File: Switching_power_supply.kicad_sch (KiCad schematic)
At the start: 28 parts, among them J8 Conn_01x03_Pin, SW1 SW_DIP_x04, U4 AMS1117, U5 LM2596HVS-ADJRG

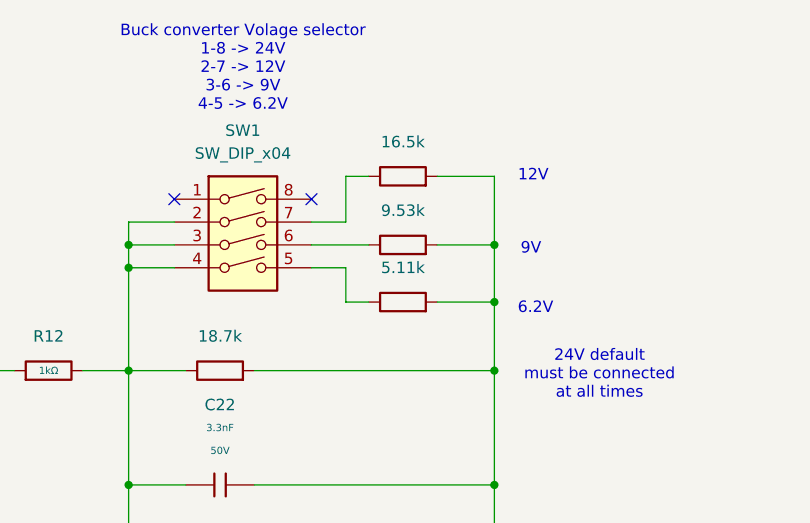
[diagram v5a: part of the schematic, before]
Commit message: Added Routing
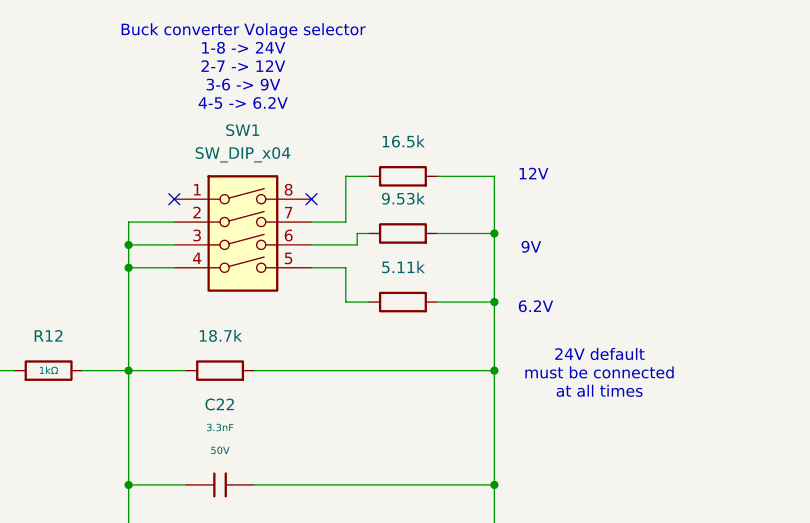
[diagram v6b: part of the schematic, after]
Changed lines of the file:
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@@
 	)
 	(junction
-		(at 195.58 66.04)
+		(at 228.6 111.76)
 		(diameter 0)
 		(color 0 0 0 0)
 	)
 	(junction
-		(at 228.6 111.76)
+		(at 200.66 111.76)
 		(diameter 0)
 		(color 0 0 0 0)
 	)
 	(junction
-		(at 200.66 111.76)
+		(at 158.75 111.76)
 		(diameter 0)
 		(color 0 0 0 0)
 	)
 	(junction
-		(at 158.75 111.76)
+		(at 195.58 64.77)
 		(diameter 0)
 		(color 0 0 0 0)
@@
 	(wire
 		(pts
+			(xy 180.34 66.04) (xy 175.26 66.04)
+		)
+		(stroke
+			(width 0)
+			(type default)
+		)
+	)
+	(wire
+		(pts
 			(xy 212.09 123.19) (xy 212.09 129.54)
 		)
@@
 	(wire
 		(pts
-			(xy 195.58 66.04) (xy 195.58 72.39)
-		)
-		(stroke
-			(width 0)
-			(type default)
-		)
-	)
-	(wire
-		(pts
 			(xy 195.58 111.76) (xy 200.66 111.76)
 		)
@@
 	(wire
 		(pts
-			(xy 189.23 66.04) (xy 195.58 66.04)
+			(xy 189.23 64.77) (xy 195.58 64.77)
 		)
 		(stroke
@@
 	(wire
 		(pts
-			(xy 195.58 58.42) (xy 195.58 66.04)
+			(xy 195.58 58.42) (xy 195.58 64.77)
 		)
 		(stroke
@@
 	(wire
 		(pts
+			(xy 195.58 64.77) (xy 195.58 72.39)
+		)
+		(stroke
+			(width 0)
+			(type default)
+		)
+	)
+	(wire
+		(pts
 			(xy 114.3 175.26) (xy 114.3 180.34)
 		)
@@
 	(wire
 		(pts
-			(xy 175.26 66.04) (xy 181.61 66.04)
+			(xy 180.34 64.77) (xy 181.61 64.77)
 		)
 		(stroke
@@
 	(wire
 		(pts
+			(xy 180.34 64.77) (xy 180.34 66.04)
+		)
+		(stroke
+			(width 0)
+			(type default)
+		)
+	)
+	(wire
+		(pts
 			(xy 200.66 129.54) (xy 200.66 135.89)
 		)
@@
 	(symbol
 		(lib_id "Device:R")
-		(at 185.42 66.04 90)
+		(at 185.42 64.77 90)
 		(unit 1)
 		(exclude_from_sim no)
@@
 		(fields_autoplaced yes)
 		(property "Reference" "R15"
-			(at 185.42 59.69 90)
+			(at 185.42 58.42 90)
 			(effects
 				(font
@@
 		)
 		(property "Value" "9.53k"
-			(at 185.42 62.23 90)
+			(at 185.42 60.96 90)
 			(effects
 				(font
@@
 		)
 		(property "Footprint" "PCM_JLCPCB:R_0402"
-			(at 185.42 67.818 90)
+			(at 185.42 66.548 90)
 			(effects
 				(font
@@
 		)
 		(property "Datasheet" "~"
-			(at 185.42 66.04 0)
+			(at 185.42 64.77 0)
 			(effects
 				(font
@@
 		)
 		(property "Description" "Resistor"
-			(at 185.42 66.04 0)
+			(at 185.42 64.77 0)
 			(effects
 				(font
@@
 		)
 		(property "LCSC" "C295883"
-			(at 185.42 66.04 90)
+			(at 185.42 64.77 90)
 			(effects
 				(font
@@
 		)
 		(property "Sim.Device" ""
-			(at 185.42 66.04 90)
+			(at 185.42 64.77 90)
 			(effects
 				(font
@@
 		)
 		(instances
-			(project "MMS2_hat_template_small"
+			(project "MMS3_hat_stepper_controler"
 				(path "/6596548a-44e0-46d8-8624-fd71cf4a3e17/c6fe6645-c1eb-4317-9e6f-134a73c9fa05"
 					(reference "R15")

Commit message: updated routing
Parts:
- added TP8: TestPoint, TestPoint:TestPoint_Pad_D1.0mm, symbol Connector:TestPoint
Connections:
- net U_reg: now also TP8.1
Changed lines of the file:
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@@
 	)
 	(junction
+		(at 259.08 111.76)
+		(diameter 0)
+		(color 0 0 0 0)
+	)
+	(junction
 		(at 106.68 124.46)
 		(diameter 0)
@@
 	(wire
 		(pts
+			(xy 259.08 111.76) (xy 266.7 111.76)
+		)
+		(stroke
+			(width 0)
+			(type default)
+		)
+	)
+	(wire
+		(pts
 			(xy 168.91 80.01) (xy 195.58 80.01)
 		)
@@
 	(wire
 		(pts
-			(xy 250.19 111.76) (xy 256.54 111.76)
+			(xy 250.19 111.76) (xy 259.08 111.76)
 		)
 		(stroke
@@
 	(wire
 		(pts
+			(xy 259.08 109.22) (xy 259.08 111.76)
+		)
+		(stroke
+			(width 0)
+			(type default)
+		)
+	)
+	(wire
+		(pts
 			(xy 200.66 111.76) (xy 212.09 111.76)
 		)
@@
 	(symbol
 		(lib_id "power:+5V")
-		(at 256.54 111.76 270)
+		(at 266.7 111.76 270)
 		(mirror x)
 		(unit 1)
@@
 		(fields_autoplaced yes)
 		(property "Reference" "#PWR090"
-			(at 252.73 111.76 0)
+			(at 262.89 111.76 0)
 			(effects
 				(font
@@
 		)
 		(property "Value" "U_reg"
-			(at 260.35 111.7599 90)
+			(at 270.51 111.7599 90)
 			(effects
 				(font
@@
 		)
 		(property "Footprint" ""
-			(at 256.54 111.76 0)
+			(at 266.7 111.76 0)
 			(effects
 				(font
@@
 		)
 		(property "Datasheet" ""
-			(at 256.54 111.76 0)
+			(at 266.7 111.76 0)
 			(effects
 				(font
@@
 		)
 		(property "Description" "Power symbol creates a global label with name \"+5V\""
-			(at 256.54 111.76 0)
+			(at 266.7 111.76 0)
 			(effects
 				(font
@@
 					(unit 1)
 				)
+			)
+		)
+	)
+	(symbol
+		(lib_id "Connector:TestPoint")
+		(at 259.08 109.22 0)
+		(unit 1)
+		(exclude_from_sim no)
+		(in_bom yes)
+		(on_board yes)
+		(dnp no)
+		(fields_autoplaced yes)
+		(property "Reference" "TP8"
+			(at 261.62 104.6479 0)
+			(effects
+				(font
+					(size 1.27 1.27)
+				)
+				(justify left)
+			)
+		)
+		(property "Value" "TestPoint"
+			(at 261.62 107.1879 0)
+			(effects
+				(font
+					(size 1.27 1.27)
+				)
+				(justify left)
+			)
+		)
+		(property "Footprint" "TestPoint:TestPoint_Pad_D1.0mm"
+			(at 264.16 109.22 0)
+			(effects
+				(font
+					(size 1.27 1.27)
+				)
+				(hide yes)
+			)
+		)
+		(property "Datasheet" "~"
+			(at 264.16 109.22 0)
+			(effects
+				(font
+					(size 1.27 1.27)
+				)
+				(hide yes)
+			)
+		)
+		(property "Description" "test point"
+			(at 259.08 109.22 0)
+			(effects
+				(font
+					(size 1.27 1.27)
+				)
+				(hide yes)
+			)
+		)
+		(pin "1"
+		)
+		(instances
+			(project "MMS3_hat_stepper_controler"
+				(path "/6596548a-44e0-46d8-8624-fd71cf4a3e17/c6fe6645-c1eb-4317-9e6f-134a73c9fa05"
+					(reference "TP8")
+					(unit 1)
+				)

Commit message: minor fixes + production files
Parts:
- added D5, D6, D7: MBRD10100CTTR, SMC_MBRD10100CTTR:TO-252-3_L6.5-W5.8-P4.58-TL, symbol SMC_MBRD10100CTTR:MBRD10100CTTR
- L1: LCSC C5368704 -> C5368704
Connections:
- net U_reg: now also D7.2 (K); no longer J8.3 (Pin_3)
- new net: D6.2 (K), D7.1, D7.3
- new net: D5.1, D5.3, J8.3 (Pin_3)
- new net: D5.2 (K), D6.1, D6.3
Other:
- note added: "Diodes to drop voltage from chainbus max 48V to 46V for TMC5130A-TA to handle"
- moved on the sheet: C17, C19, C20, C21, C22, C23, C24, C25, C26, C27, C28, D4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
